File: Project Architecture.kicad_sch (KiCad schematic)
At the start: 0 parts

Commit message: [Schématique test]
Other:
- sheet Converteur_3.3VD renamed Converteur_3.3V a 6V
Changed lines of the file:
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@@
 			(color 255 200 0 0.5020)
 		)
-		(property "Sheetname" "Converteur_3.3VD"
+		(property "Sheetname" "Converteur_3.3V a 6V"
 			(at 138.43 110.7309 0)
 			(effects

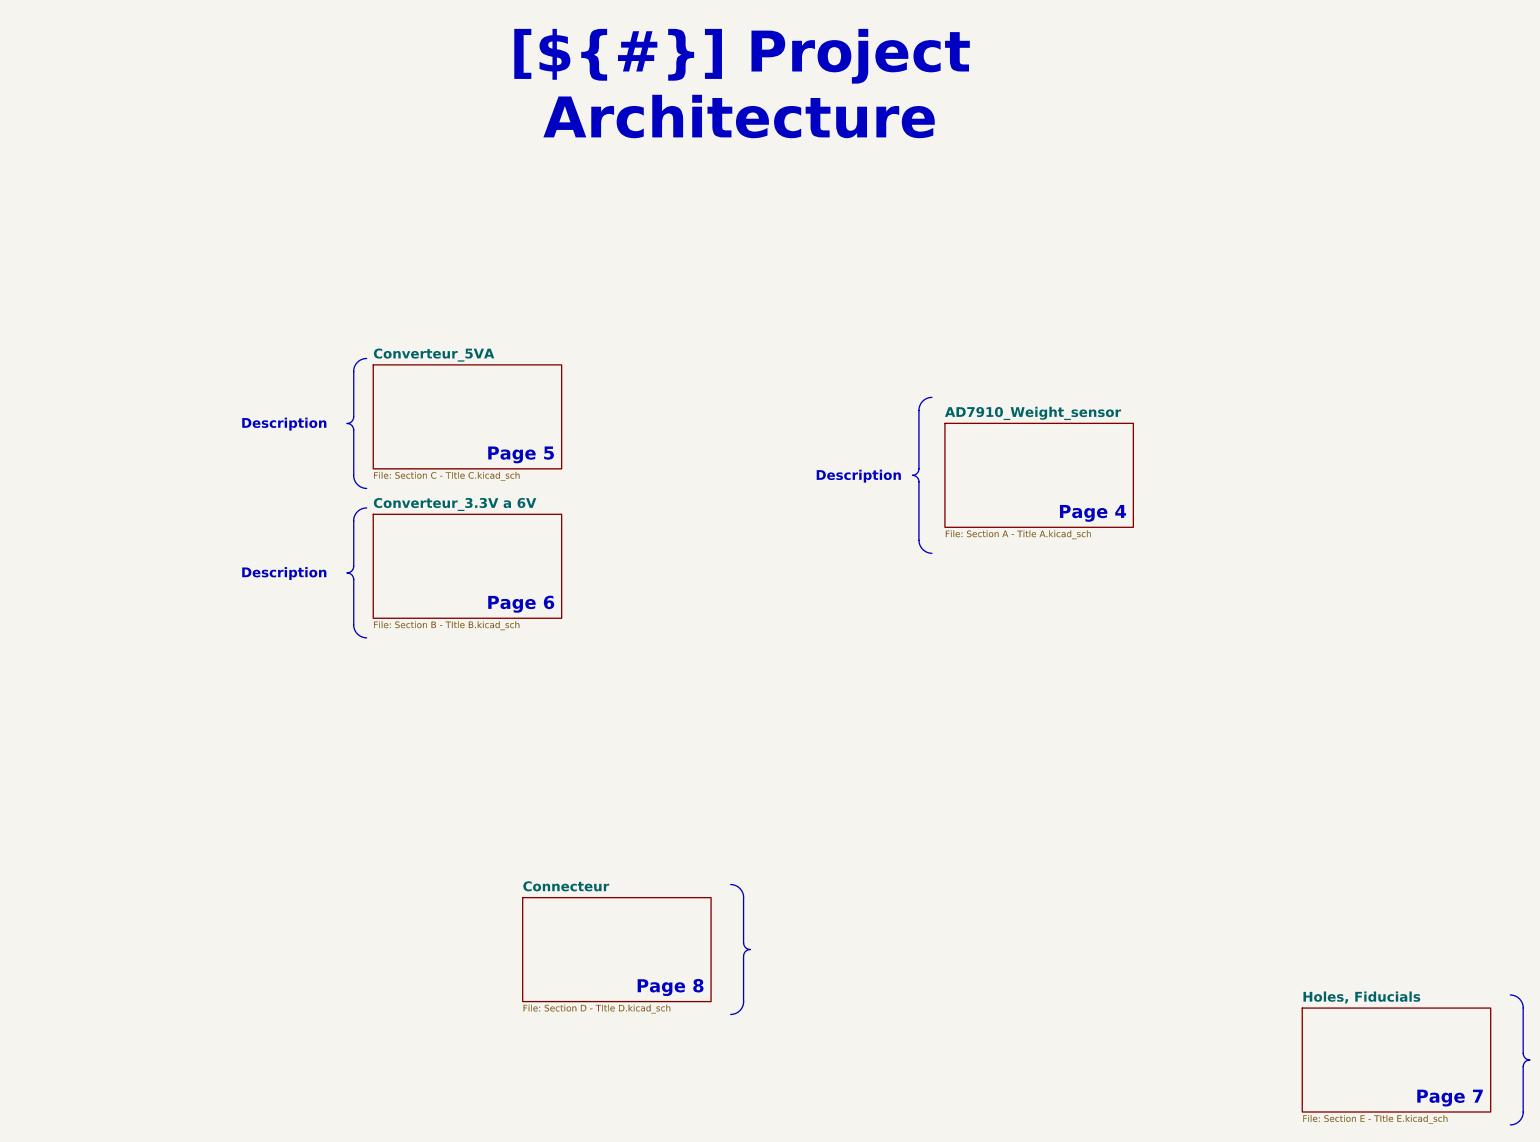
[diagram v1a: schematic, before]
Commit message: [FINISH LT3042 and ad TPS6108]
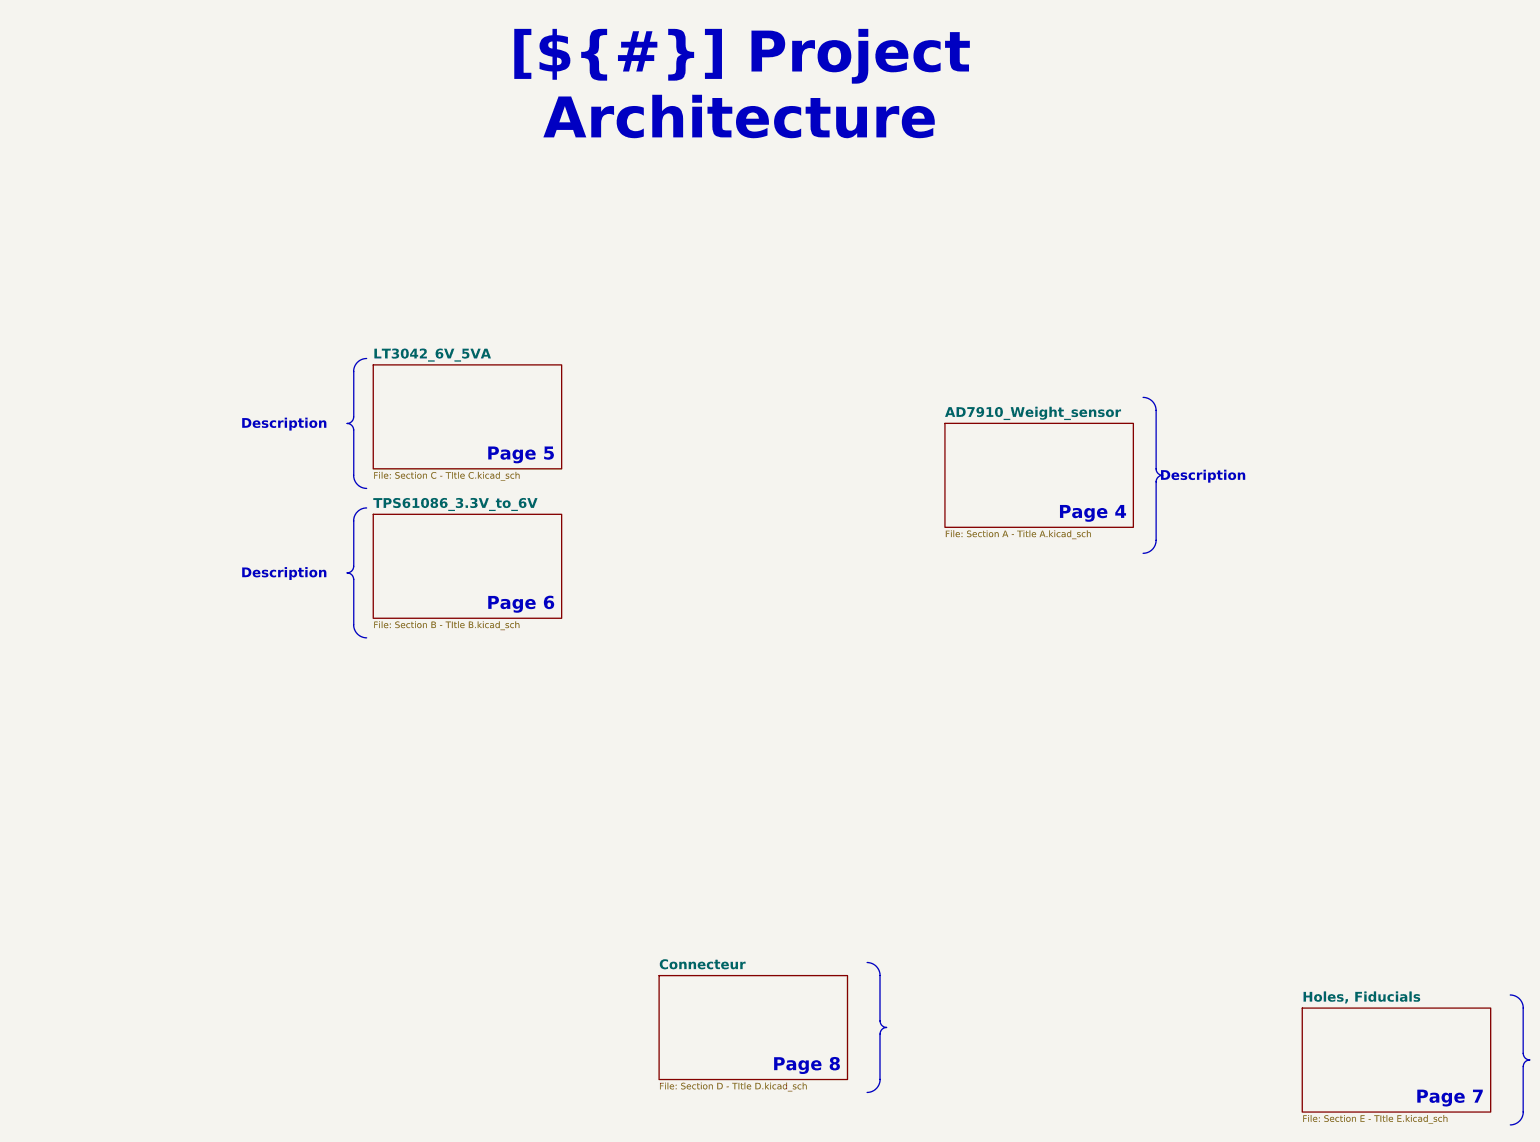
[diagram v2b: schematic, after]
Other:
- sheet Converteur_3.3V a 6V renamed TPS61086_3.3V_to_6V
- sheet Converteur_5VA renamed LT3042_6V_5VA
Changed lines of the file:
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@@
 	)
 	(arc
-		(start 212.11 196.83)
-		(mid 211.2149 196.4551)
-		(end 210.84 195.56)
-		(stroke
-			(width 0)
-			(type default)
-		)
-		(fill
-			(type none)
-		)
-	)
-	(arc
-		(start 245.11 102.87)
-		(mid 244.7351 103.7651)
-		(end 243.84 104.14)
+		(start 238.78 212.07)
+		(mid 237.8849 211.6951)
+		(end 237.51 210.8)
+		(stroke
+			(width 0)
+			(type default)
+		)
+		(fill
+			(type none)
+		)
+	)
+	(arc
+		(start 291.465 105.41)
+		(mid 291.8399 104.5149)
+		(end 292.735 104.14)
 		(stroke
 			(width 0)
@@
 	)
 	(arc
-		(start 243.84 104.14)
-		(mid 244.7351 104.5149)
-		(end 245.11 105.41)
-		(stroke
-			(width 0)
-			(type default)
-		)
-		(fill
-			(type none)
-		)
-	)
-	(arc
-		(start 247.65 119.38)
-		(mid 245.8598 118.6302)
-		(end 245.11 116.84)
+		(start 292.735 104.14)
+		(mid 291.8399 103.7651)
+		(end 291.465 102.87)
+		(stroke
+			(width 0)
+			(type default)
+		)
+		(fill
+			(type none)
+		)
+	)
+	(arc
+		(start 288.925 88.9)
+		(mid 290.7152 89.6498)
+		(end 291.465 91.44)
 		(stroke
 			(width 0)
@@
 	)
 	(arc
-		(start 210.84 206.99)
-		(mid 210.0961 208.7861)
-		(end 208.3 209.53)
+		(start 237.51 222.23)
+		(mid 236.7661 224.0261)
+		(end 234.97 224.77)
 		(stroke
 			(width 0)
@@
 	)
 	(arc
-		(start 210.84 198.1)
-		(mid 211.2149 197.2049)
-		(end 212.11 196.83)
+		(start 237.51 213.34)
+		(mid 237.8849 212.4449)
+		(end 238.78 212.07)
 		(stroke
 			(width 0)
@@
 	)
 	(arc
-		(start 208.3 184.13)
-		(mid 210.0902 184.8798)
-		(end 210.84 186.67)
-		(stroke
-			(width 0)
-			(type default)
-		)
-		(fill
-			(type none)
-		)
-	)
-	(arc
-		(start 245.11 91.44)
-		(mid 245.8539 89.6439)
-		(end 247.65 88.9)
+		(start 234.97 199.37)
+		(mid 236.7602 200.1198)
+		(end 237.51 201.91)
+		(stroke
+			(width 0)
+			(type default)
+		)
+		(fill
+			(type none)
+		)
+	)
+	(arc
+		(start 291.465 116.84)
+		(mid 290.7211 118.6361)
+		(end 288.925 119.38)
 		(stroke
 			(width 0)
@@
 	(text "Page 8"
 		(exclude_from_sim no)
-		(at 203.2 205.74 0)
+		(at 229.87 220.98 0)
 		(effects
 			(font
@@
 	(text_box "Description"
 		(exclude_from_sim no)
-		(at 226.06 101.6 0)
-		(size 17.145 5.08)
+		(at 310.515 106.68 0)
+		(size -17.145 -5.08)
 		(margins 1.4287 1.4287 1.4287 1.4287)
 		(stroke
@@
 	(polyline
 		(pts
-			(xy 245.11 105.41) (xy 245.11 116.84)
+			(xy 291.465 102.87) (xy 291.465 91.44)
 		)
 		(stroke
@@
 	(polyline
 		(pts
-			(xy 245.11 102.87) (xy 245.11 91.44)
+			(xy 291.465 105.41) (xy 291.465 116.84)
 		)
 		(stroke
@@
 	(polyline
 		(pts
-			(xy 210.82 186.69) (xy 210.82 195.58)
+			(xy 237.49 201.93) (xy 237.49 210.82)
 		)
 		(stroke
@@
 	(polyline
 		(pts
-			(xy 210.82 198.12) (xy 210.82 207.01)
+			(xy 237.49 213.36) (xy 237.49 222.25)
 		)
 		(stroke
@@
 			(color 255 200 0 0.5020)
 		)
-		(property "Sheetname" "Converteur_3.3V a 6V"
+		(property "Sheetname" "TPS61086_3.3V_to_6V"
 			(at 138.43 110.7309 0)
 			(effects
@@
 	)
 	(sheet
-		(at 167.64 186.69)
+		(at 194.31 201.93)
 		(size 36.83 20.32)
 		(exclude_from_sim no)
@@
 		)
 		(property "Sheetname" "Connecteur"
-			(at 167.64 185.6609 0)
+			(at 194.31 200.9009 0)
 			(effects
 				(font
@@
 		)
 		(property "Sheetfile" "Section D - TItle D.kicad_sch"
-			(at 167.64 207.5946 0)
+			(at 194.31 222.8346 0)
 			(effects
 				(font
@@
 			(color 255 200 0 0.5020)
 		)
-		(property "Sheetname" "Converteur_5VA"
+		(property "Sheetname" "LT3042_6V_5VA"
 			(at 138.43 81.5209 0)
 			(effects

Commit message: [ADD TPS6108]
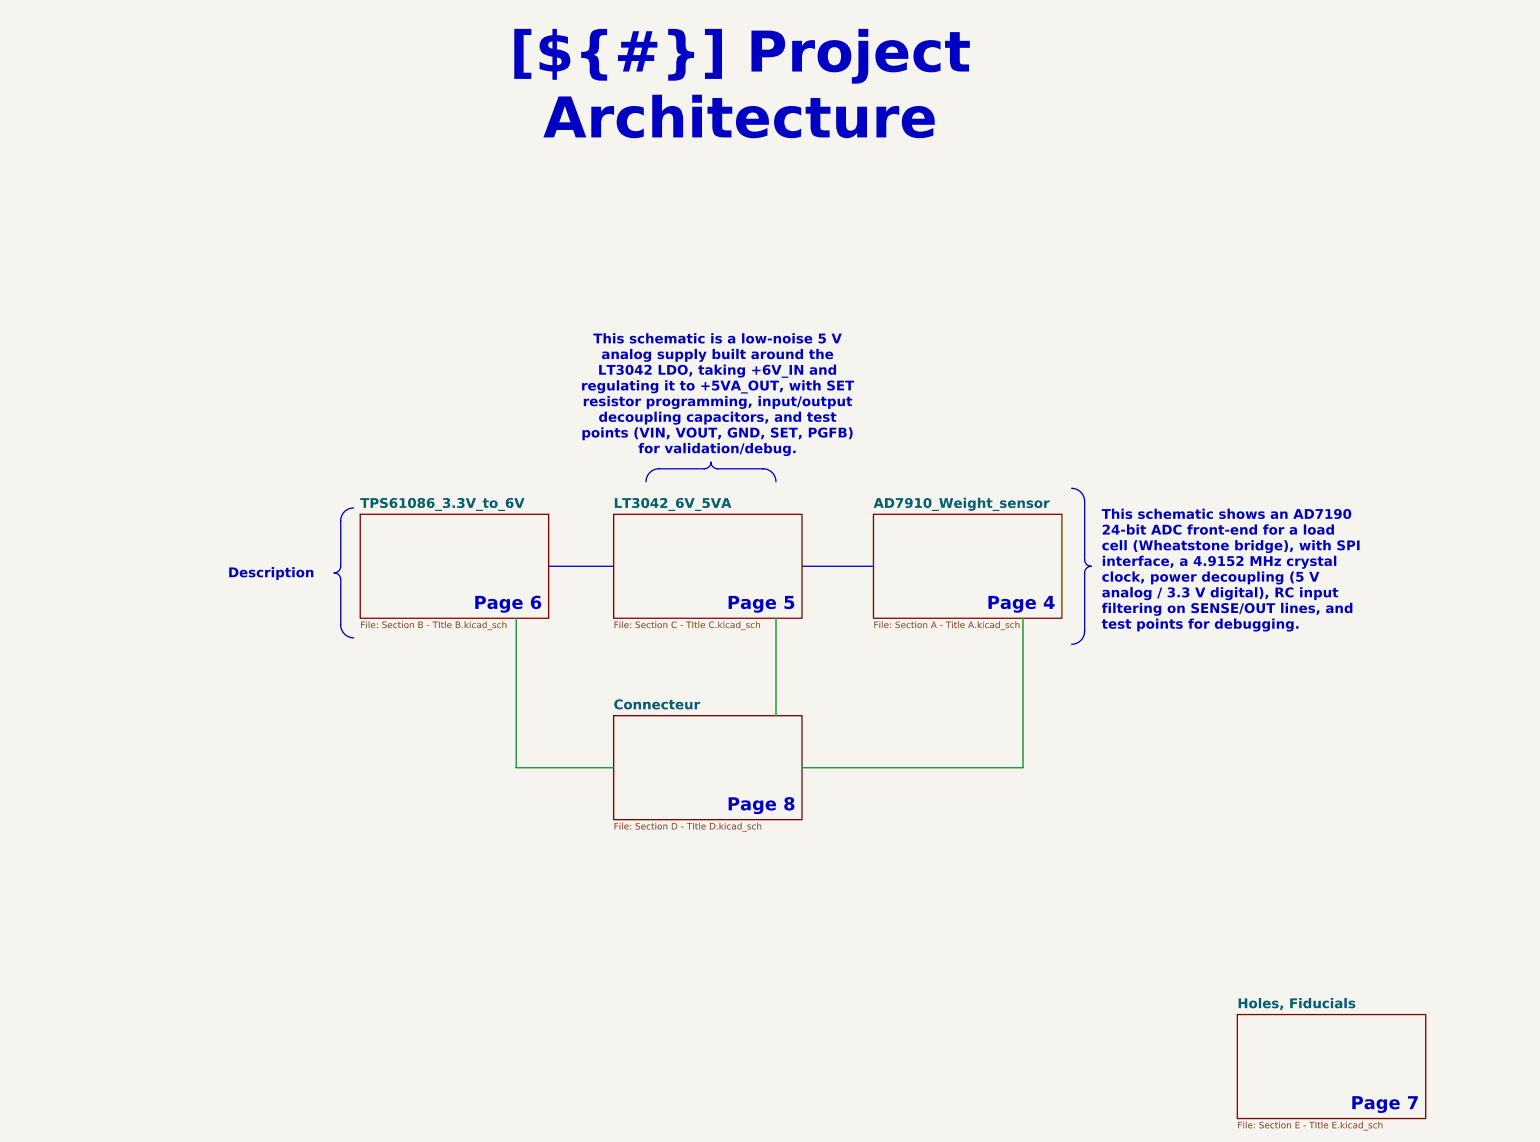
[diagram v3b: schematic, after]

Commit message: [Finish schématiq]
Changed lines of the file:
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@@
 		)
 	)
-	(text_box "Description"
+	(text_box "This schematic is a TPS61086-based 3.3 V → 6 V boost supply with inductor/Schottky power stage, feedback divider for VOUT, decoupling + soft-start/compensation, and test points (+3.3V_IN, +6V_OUT, FB, GND)."
 		(exclude_from_sim no)
-		(at 108.605 120.63 0)
-		(size 26.015 5.1)
+		(at 66.04 113.01 0)
+		(size 64.77 12.72)
 		(margins 1.4287 1.4287 1.4287 1.4287)
 		(stroke
 			(width -0.0001)
-			(type default)
+			(type solid)
 		)
 		(fill

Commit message: [PCB V3]
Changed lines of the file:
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@@
 		)
 	)
-	(text_box "This schematic is a TPS61086-based 3.3 V → 6 V boost supply with inductor/Schottky power stage, feedback divider for VOUT, decoupling + soft-start/compensation, and test points (+3.3V_IN, +6V_OUT, FB, GND)."
-		(exclude_from_sim no)
-		(at 66.04 113.01 0)
-		(size 64.77 12.72)
+	(text_box "3.3 V to 6 V synchronous boost converter supplying the LT3042 LDO stage.\nTPS61086 switching at 1.2 MHz (fixed frequency, PWM/PFM selectable via MODE). Integrated 2.5 A / 0.13 Ω power switch. Output voltage set via FB resistor divider. Input/output decoupling, soft-start, and loop compensation network. Test points: +3.3V_IN, +6V_OUT, FB, COMP."
+		(exclude_from_sim no)
+		(at 73.66 113.01 0)
+		(size 57.15 12.72)
 		(margins 1.4287 1.4287 1.4287 1.4287)
 		(stroke
@@
 		(effects
 			(font
-				(size 1.905 1.905)
+				(size 1.27 1.27)
 				(thickness 0.381)
 				(bold yes)
@@
 		)
 	)
-	(text_box "This schematic shows an AD7190 24-bit ADC front-end for a load cell (Wheatstone bridge), with SPI interface, a 4.9152 MHz crystal clock, power decoupling (5 V analog / 3.3 V digital), RC input filtering on SENSE/OUT lines, and test points for debugging."
+	(text_box "AD7190 24-bit sigma-delta ADC front-end for Wheatstone bridge acquisition.\nDifferential inputs on SENSE± and OUT± lines with RC input filtering. SPI interface (CS, DIN, DOUT, SCLK, SYNC). External 4.9152 MHz crystal clock. Dual-supply decoupling (+5VA analog / +3.3V digital). P-MOS drive gate for load cell excitation control. Test points on all critical analog and digital nodes."
 		(exclude_from_sim no)
 		(at 279.4 109.22 0)
-		(size 53.34 5.08)
+		(size 45.72 5.08)
 		(margins 1.4287 1.4287 1.4287 1.4287)
 		(stroke
@@
 		(effects
 			(font
-				(size 1.905 1.905)
+				(size 1.27 1.27)
 				(thickness 0.381)
 				(bold yes)
@@
 		)
 	)
-	(text_box "This schematic is a low-noise 5 V analog supply built around the LT3042 LDO, taking +6V_IN and regulating it to +5VA_OUT, with SET resistor programming, input/output decoupling capacitors, and test points (VIN, VOUT, GND, SET, PGFB) for validation/debug."
-		(exclude_from_sim no)
-		(at 176.53 74.91 0)
+	(text_box "Low-noise 5 V analog supply for ADC front-end (AVDD).\nLT3042 ultralow-noise LDO regulator (PSRR > 75 dB). Input: +6V from boost stage. Output: +5VA regulated via RSET = 50 kΩ (ISET = 100 µA). Solid tantalum capacitor on SET pin for noise suppression. Power-Good monitoring via PGFB divider. Test points: VIN, VOUT, SET, PGFB, PG."
+		(exclude_from_sim no)
+		(at 176.53 82.53 0)
 		(size 58.42 5.1)
 		(margins 1.4287 1.4287 1.4287 1.4287)
@@
 		(effects
 			(font
-				(size 1.905 1.905)
+				(size 1.27 1.27)
 				(thickness 0.381)
 				(bold yes)
@@
 		(stroke
 			(width 0)
-			(type dot)
+			(type solid)
 		)
 	)
@@
 		(stroke
 			(width 0)
-			(type dot)
-		)
-	)
-	(wire
-		(pts
-			(xy 217.17 132.08) (xy 217.17 151.13)
-		)
-		(stroke
-			(width 0)
-			(type dot)
+			(type solid)
 		)
 	)
@@
 		)
 		(fill
-			(color 255 200 0 0.5020)
+			(color 157 191 255 1.0000)
 		)
 		(property "Sheetname" "TPS61086_3.3V_to_6V"
@@
 		)
 		(fill
-			(color 255 200 0 0.5020)
+			(color 157 191 255 1.0000)
 		)
 		(property "Sheetname" "LT3042_6V_5VA"
